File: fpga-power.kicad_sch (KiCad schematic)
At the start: 76 parts, among them U8 XC7K160T-FFG676

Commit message: [#65754] Rev 2.0.0 Initial commit - source design files from so-dimm-ddr5-tester e0a54f86
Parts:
- removed C100, C104, C114, C116, C118, C47, C51, C55, C57, C59, C61, C63, C65, C66, C67, C69, C70, C71, C73, C74, C75, C77, C78, C79, C81, C82, C83, C84, C85, C87, C88, C89, C91, C92, C93, C95, C96, C97, C98: C_100n_0201, data-center-rdimm-ddr5-tester-footprints:C_0201, symbol data-center-rdimm-ddr5-tester:C_100n_0201
- removed C101, C106, C107, C108, C109, C110, C111, C113, C115, C117, C48, C50, C52, C54, C56, C58, C62, C68, C72, C76, C80, C86, C90, C94, C99: C_4u7_0402, data-center-rdimm-ddr5-tester-footprints:C_0402_1005Metric, symbol data-center-rdimm-ddr5-tester:C_4u7_0402
- removed C102, C105: C_330u_KEMET_D, data-center-rdimm-ddr5-tester-footprints:KEMET_D, symbol data-center-rdimm-ddr5-tester:C_330u_KEMET_D
- removed C103, C119, C120, C121, C49, C53, C60, C64: C_47u_0603, data-center-rdimm-ddr5-tester-footprints:C_0603_1608Metric, symbol data-center-rdimm-ddr5-tester:C_47u_0603
- removed C112: C_100u_KEMET_A, data-center-rdimm-ddr5-tester-footprints:KEMET_A, symbol data-center-rdimm-ddr5-tester:C_100u_KEMET_A
- removed U8: XC7K160T-FFG676, data-center-rdimm-ddr5-tester-footprints:BGA-676_27x27mm_Layout26x26_P1X1mm, symbol data-center-rdimm-ddr5-tester:XC7K160T-FFG676
- added C100, C101, C104, C105, C106, C107, C108, C13, C19, C20, C21, C22, C23, C24, C26, C28, C29, C30, C31, C32, C33, C35, C36, C37, C39, C40, C41, C42, C44, C45, C46, C47, C48, C49, C51, C52, C53, C55, C56, C58, C59, C61, C63, C64, C65, C66, C68, C69, C70, C72, C74, C75, C76, C77, C78, C79, C80, C81, C82, C83, C84, C86, C87, C88, C89, C90, C91, C92, C93, C94, C95, C96, C98, C99: C_100n_0402, antmicro-footprints:C_0402_1005Metric, symbol antmicroCapacitors0402:C_100n_0402
- added C102, C103, C34, C43, C50, C57, C62, C67, C71, C97: C_4u7_0402, antmicro-footprints:C_0402_1005Metric, symbol antmicroCapacitors0402:C_4u7_0402
- added C11, C14, C15, C16, C17, C18, C27, C60, C73, C85: C_47u_0603, antmicro-footprints:C_0603_1608Metric, symbol antmicroCapacitors0603:C_47u_0603
- added C12: C_Pol_1m_2.5V_KEMET-T520-D, antmicro-footprints:C_Pol_EIA-D, symbol antmicroCapacitorspol:C_Pol_1m_2.5V_KEMET-T520-D
- added C25, C38: C_Pol_330u_6.3V_KEMET-T520-B, antmicro-footprints:C_Pol_EIA-B, symbol antmicroCapacitorspol:C_Pol_330u_6.3V_KEMET-T520-B
- added C54: C_100u_0805, antmicro-footprints:C_0805_2012Metric, symbol antmicroCapacitorsmisc:C_100u_0805
- added R39: R_100R_0402, antmicro-footprints:R_0402_1005Metric, symbol antmicroResistors0402:R_100R_0402
- added U4: XC7K160T-FFG676, antmicro-footprints:BGA-676_27x27mm_Layout26x26_P1x1mm_FFG676, symbol antmicroFPGAChips:XC7K160T-FFG676
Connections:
- net GND: now also C100.1, C101.1, C102.2, C103.2, C104.1, C105.1, C106.1, C107.1, C108.1, C11.2, C12.2, C13.1, C14.2, C15.2, C16.2, C17.2, C18.2, C19.1, C20.1, C21.1, C22.1, C23.1, C24.1, C25.2, C26.1, C27.2, C28.1, C29.1, C30.1, C31.1, C32.1, C33.1, C34.2, C35.1, C36.1, C37.1, C38.2, C39.1, C40.1, C41.1, C42.1, C43.2, C44.1, C45.1, C46.1, C47.1, C48.1, C49.1, C50.2, C51.1, C52.1, C53.1, C54.1, C55.1, C56.1, C57.2, C58.1, C59.1, C60.2, C61.1, C62.2, C63.1, C64.1, C65.1, C66.1, C67.2, C68.1, C69.1, C70.1, C71.2, C72.1, C73.2, C74.1, C75.1, C76.1, C77.1, C78.1, C79.1, C80.1, C81.1, C82.1, C83.1, C84.1, C85.2, C86.1, C87.1, C88.1, C89.1, C90.1, C91.1, C92.1, C93.1, C94.1, C95.1, C96.1, C97.2, C98.1, C99.1, U4.A1 (GND), U4.A16 (GND), U4.A2 (GND), U4.A26 (GND), U4.A5 (GND), U4.A6 (GND), U4.A7 (GND), U4.AA16 (GND), U4.AA26 (GND), U4.AA6 (GND), U4.AB13 (GND), U4.AB23 (GND), U4.AB3 (GND), U4.AC10 (GND), U4.AC20 (GND), U4.AD17 (GND), U4.AD7 (GND), U4.AE14 (GND), U4.AE24 (GND), U4.AE4 (GND), U4.AF1 (GND), U4.AF11 (GND), U4.AF21 (GND), U4.B13 (GND), U4.B23 (GND), U4.B4 (GND), U4.B7 (GND), U4.C1 (GND), U4.C10 (GND), U4.C20 (GND), U4.C5 (GND), U4.C7 (GND), U4.D17 (GND), U4.D4 (GND), U4.D7 (GND), U4.E1 (GND), U4.E14 (GND), U4.E2 (GND), U4.E24 (GND), U4.E5 (GND), U4.E7 (GND), U4.F11 (GND), U4.F21 (GND), U4.F3 (GND), U4.F4 (GND), U4.F7 (GND), U4.G1 (GND), U4.G18 (GND), U4.G5 (GND), U4.G8 (GND), U4.H15 (GND), U4.H25 (GND), U4.H4 (GND), U4.H7 (GND), U4.J1 (GND), U4.J12 (GND), U4.J2 (GND), U4.J22 (GND), U4.J5 (GND), U4.K11 (GND), U4.K13 (GND), U4.K19 (GND), U4.K3 (GND), U4.K4 (GND), U4.K7 (GND), U4.K9 (GND), U4.L1 (GND), U4.L10 (GND), U4.L12 (GND), U4.L14 (GND), U4.L16 (GND), U4.L26 (GND), U4.L5 (GND), U4.M11 (GNDADC_0), U4.M13 (GND), U4.M15 (GND), U4.M23 (GND), U4.M4 (GND), U4.M7 (GND), U4.M9 (GND), U4.N1 (GND), U4.N10 (GND), U4.N14 (GND), U4.N2 (GND), U4.N20 (GND), U4.N5 (GND), U4.N7 (GND), U4.P13 (GND), U4.P15 (GND), U4.P17 (GND), U4.P3 (GND), U4.P4 (GND), U4.P9 (GND), U4.R1 (GND), U4.R10 (GND), U4.R14 (GND), U4.R2 (GND), U4.R24 (GND), U4.R5 (GND), U4.R8 (GND), U4.T1 (GND), U4.T11 (GND), U4.T13 (GND), U4.T15 (GND), U4.T21 (GND), U4.T3 (GND), U4.T4 (GND), U4.T9 (GND), U4.U10 (GND), U4.U12 (GND), U4.U14 (GND), U4.U18 (GND), U4.U8 (GND), U4.V15 (GND), U4.V25 (GND), U4.V5 (GND), U4.W12 (GND), U4.W2 (GND), U4.W22 (GND), U4.Y19 (GND), U4.Y9 (GND)
- new net: R39.1, U4.M6 (MGTRREF_115)
- new net +1V0: C12.1, C13.2, C19.2, C25.1, C26.2, C33.2, C38.1, C42.2, C48.2, C54.2, C55.2, C61.2, C62.1, C65.2, C67.1, C70.2, C71.1, C75.2, C79.2, C83.2, C86.2, C88.2, C90.2, C92.2, U4.J9 (VCCINT), U4.K10 (VCCINT), U4.K12 (VCCINT), U4.K14 (VCCINT), U4.K8 (VCCINT), U4.L13 (VCCINT), U4.L15 (VCCINT), U4.L9 (VCCINT), U4.M14 (VCCINT), U4.M8 (VCCINT), U4.N13 (VCCBRAM), U4.N15 (VCCINT), U4.N9 (VCCINT), U4.P14 (VCCINT), U4.R13 (VCCBRAM), U4.R15 (VCCINT), U4.T12 (VCCBRAM), U4.T14 (VCCINT), U4.U13 (VCCBRAM), U4.U15 (VCCINT)
- new net +1V0_MGTAVCC: C100.2, C101.2, C102.1, C98.2, C99.2, U4.C6 (MGTAVCC), U4.E6 (MGTAVCC), U4.G6 (MGTAVCC), U4.J6 (MGTAVCC), U4.L6 (MGTAVCC)
- new net +1V1: C14.1, C20.2, C24.2, C31.2, C37.2, C44.2, C49.2, C60.1, C63.2, C66.2, C69.2, C74.2, C78.2, C82.2, C85.1, C87.2, C89.2, C91.2, C93.2, C94.2, C95.2
- new net +1V2_MGTAVTT: C103.1, C104.2, C105.2, C106.2, C107.2, C108.2, R39.2, U4.B3 (MGTAVTT), U4.C2 (MGTAVTT), U4.D3 (MGTAVTT), U4.G2 (MGTAVTT), U4.H3 (MGTAVTT), U4.L2 (MGTAVTT), U4.M3 (MGTAVTT), U4.M5 (MGTAVTTRCAL_115)
- new net +1V8: C11.1, C18.1, C27.1, C34.1, C43.1, C50.1, C57.1, C64.2, C68.2, C72.2, C77.2, C81.2, C84.2, C96.2, C97.1, U4.E8 (VCCBATT_0), U4.L11 (VCCAUX), U4.M10 (VCCAUX), U4.M12 (VCCADC_0), U4.N6 (MGTVCCAUX), U4.P10 (VCCAUX), U4.P8 (VCCAUX_IO_G0), U4.R9 (VCCAUX_IO_G0), U4.T10 (VCCAUX), U4.T8 (VCCAUX_IO_G0), U4.U11 (VCCAUX)
- new net +3V3: C15.1, C16.1, C17.1, C21.2, C22.2, C23.2, C28.2, C29.2, C30.2, C32.2, C35.2, C36.2, C39.2, C40.2, C41.2, C45.2, C46.2, C47.2, C51.2, C52.2, C53.2, C56.2, C58.2, C59.2, C73.1, C76.2, C80.2
- no-connect marks 45 -> 0
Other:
- note added: "BANK 0"
- note added: "BANK 12"
- note added: "BANK 14"
- note added: "BANK 16"
- note added: "BANK 32"
- note added: "BANK 33"
- note added: "BANK 34"
- note added: "Bank marked by dahed line referenced from 7 Series FPGAs PCB Design Guide UG483 (FFG+FBG Package worst case)"
- note added: "FPGA Power rails"
- note added: "MGT decoupling marked by dahed line referenced from 7 Series FPGAs PCB Design Guide UG482 (FFG+FBG Package worst case)"
- note added: "Trace length from the resistor pins to the FPGA pins MGTRREF and MGTAVTTRCAL must be equal in length."
- note added: "V_{CCAUX}"
- note added: "V_{CCBRAM}"
- note added: "V_{CCINT}"
- note removed: "Added capacitors coresponding to PCB Design Guide UG483"
- note removed: "Decoupling referenced from 7 Series FPGAs PCB Design Guide UG483 TODO: verify!"
- note removed: "POWER RAILS"
- note removed: "Place close to FPGA banks power supply"
- note removed: "UNUSED"
- title: Data Center RDIMM DDR5 Tester -> SO-DIMM DDR5 Tester

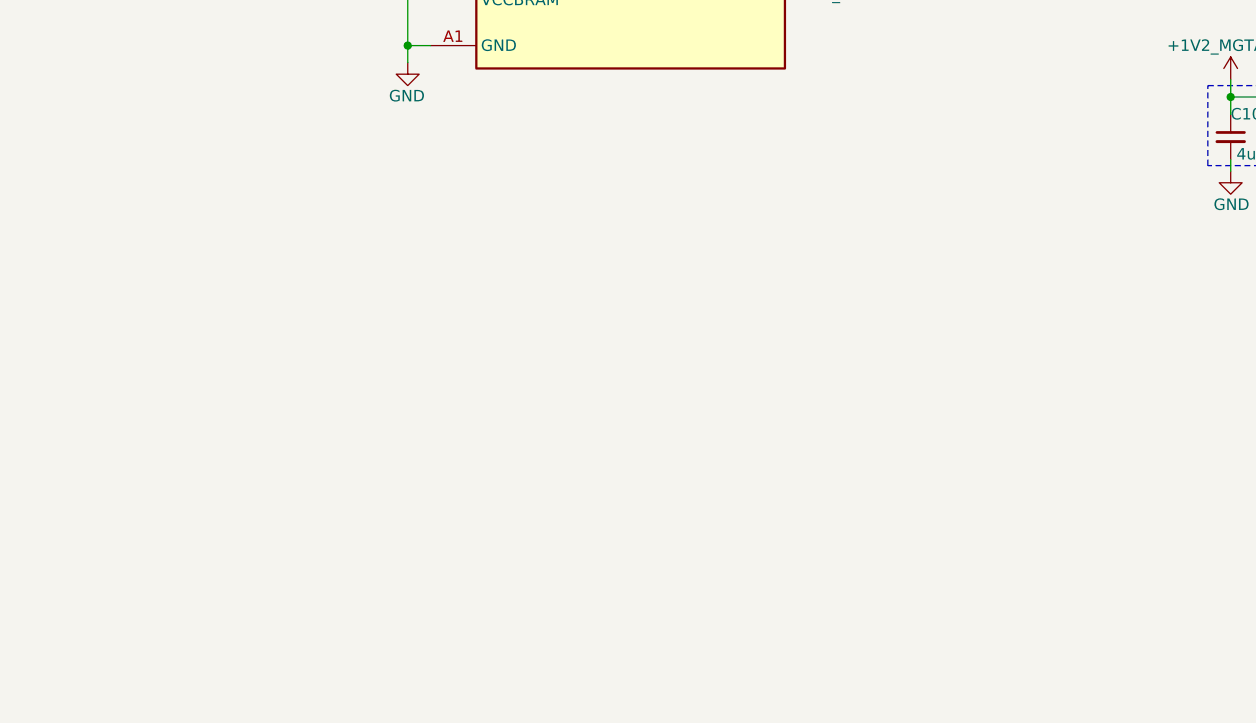
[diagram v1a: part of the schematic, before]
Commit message: [#66300] Add recommended FPGA supply voltages
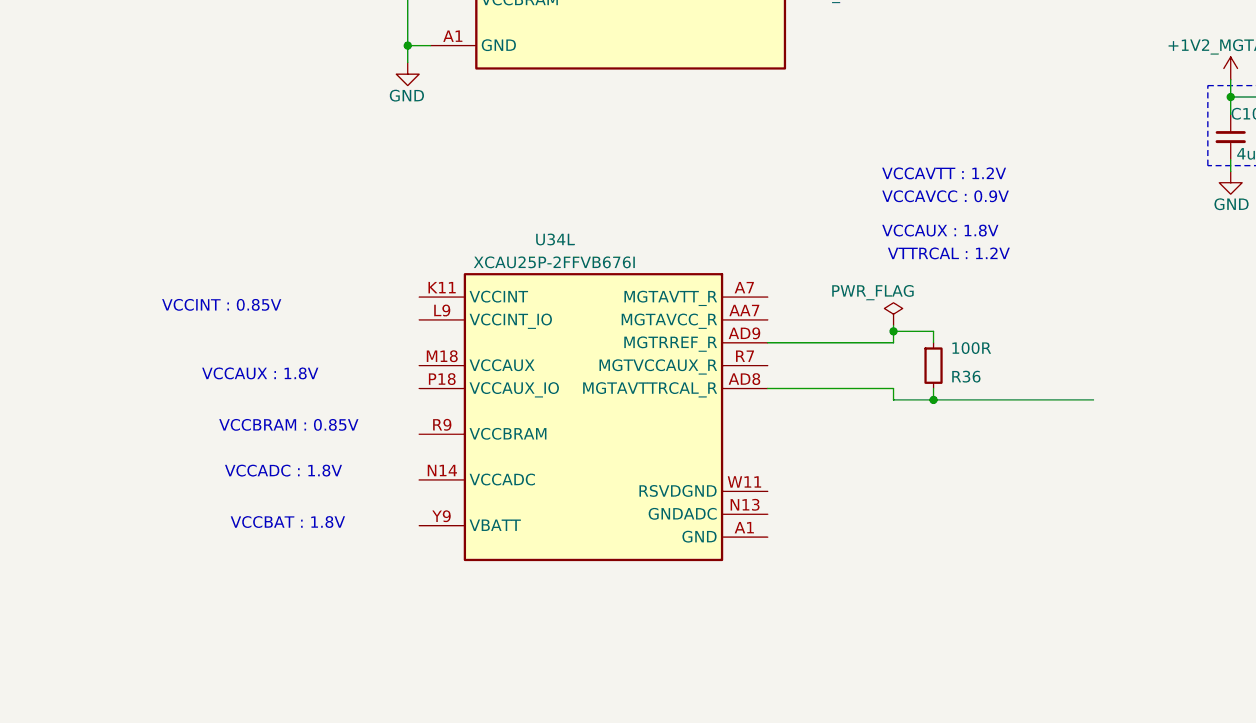
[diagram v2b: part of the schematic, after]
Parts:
- added R36: R_100R_0402, antmicro-footprints:R_0402_1005Metric, symbol antmicroResistors0402:R_100R_0402
- added U34: XCAU25P-2FFVB676I, antmicro-footprints:BGA-676_27x27mm_Layout26x26_P1x1mm_FFVB676, symbol antmicroFPGAChips:XCAU25P-2FFVB676I
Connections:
- new net: U34.A1 (GND), U34.A11 (GND), U34.A16 (GND), U34.A2 (GND), U34.A21 (GND), U34.A26 (GND), U34.A5 (GND), U34.A6 (GND), U34.A8 (GND), U34.AA1 (GND), U34.AA16 (GND), U34.AA2 (GND), U34.AA26 (GND), U34.AA3 (GND), U34.AA6 (GND), U34.AA8 (GND), U34.AB13 (GND), U34.AB23 (GND), U34.AB3 (GND), U34.AB4 (GND), U34.AB8 (GND), U34.AC1 (GND), U34.AC10 (GND), U34.AC2 (GND), U34.AC20 (GND), U34.AC25 (GND), U34.AC3 (GND), U34.AC6 (GND), U34.AC8 (GND), U34.AC9 (GND), U34.AD10 (GND), U34.AD17 (GND), U34.AD3 (GND), U34.AD4 (GND), U34.AD5 (GND), U34.AE1 (GND), U34.AE10 (GND), U34.AE14 (GND), U34.AE19 (GND), U34.AE2 (GND), U34.AE24 (GND), U34.AE5 (GND), U34.AE6 (GND), U34.AF10 (GND), U34.AF11 (GND), U34.AF16 (GND), U34.AF21 (GND), U34.AF26 (GND), U34.AF3 (GND), U34.AF4 (GND), U34.AF5 (GND), U34.AF8 (GND), U34.AF9 (GND), U34.B13 (GND), U34.B18 (GND), U34.B23 (GND), U34.B3 (GND), U34.B4 (GND), U34.B5 (GND), U34.B8 (GND), U34.C1 (GND), U34.C10 (GND), U34.C15 (GND), U34.C2 (GND), U34.C25 (GND), U34.C5 (GND), U34.C6 (GND), U34.C8 (GND), U34.D12 (GND), U34.D22 (GND), U34.D3 (GND), U34.D4 (GND), U34.D5 (GND), U34.D8 (GND), U34.E1 (GND), U34.E19 (GND), U34.E2 (GND), U34.E3 (GND), U34.E6 (GND), U34.E8 (GND), U34.F11 (GND), U34.F16 (GND), U34.F21 (GND), U34.F26 (GND), U34.F3 (GND), U34.F4 (GND), U34.F8 (GND), U34.G1 (GND), U34.G13 (GND), U34.G2 (GND), U34.G23 (GND), U34.G3 (GND), U34.G6 (GND), U34.G8 (GND), U34.H20 (GND), U34.H3 (GND), U34.H4 (GND), U34.H8 (GND), U34.J1 (GND), U34.J17 (GND), U34.J2 (GND), U34.J3 (GND), U34.J6 (GND), U34.J8 (GND), U34.K12 (GND), U34.K14 (GND), U34.K16 (GND), U34.K19 (GND), U34.K24 (GND), U34.K3 (GND), U34.K4 (GND), U34.K8 (GND), U34.L1 (GND), U34.L11 (GND), U34.L13 (GND), U34.L15 (GND), U34.L17 (GND), U34.L2 (GND), U34.L21 (GND), U34.L26 (GND), U34.L3 (GND), U34.L6 (GND), U34.L8 (GND), U34.M10 (GND), U34.M12 (GND), U34.M14 (GND), U34.M16 (GND), U34.M23 (GND), U34.M3 (GND), U34.M4 (GND), U34.M8 (GND), U34.N1 (GND), U34.N11 (GND), U34.N15 (GND), U34.N17 (GND), U34.N2 (GND), U34.N20 (GND), U34.N25 (GND), U34.N3 (GND), U34.N6 (GND), U34.N8 (GND), U34.P10 (GND), U34.P12 (GND), U34.P16 (GND), U34.P3 (GND), U34.P4 (GND), U34.P8 (GND), U34.R1 (GND), U34.R11 (GND), U34.R15 (GND), U34.R17 (GND), U34.R19 (GND), U34.R2 (GND), U34.R24 (GND), U34.R3 (GND), U34.R6 (GND), U34.R8 (GND), U34.T10 (GND), U34.T12 (GND), U34.T16 (GND), U34.T21 (GND), U34.T26 (GND), U34.T3 (GND), U34.T4 (GND), U34.T8 (GND), U34.U1 (GND), U34.U11 (GND), U34.U13 (GND), U34.U15 (GND), U34.U17 (GND), U34.U18 (GND), U34.U2 (GND), U34.U3 (GND), U34.U6 (GND), U34.U8 (GND), U34.V10 (GND), U34.V12 (GND), U34.V14 (GND), U34.V16 (GND), U34.V20 (GND), U34.V25 (GND), U34.V3 (GND), U34.V4 (GND), U34.V8 (GND), U34.W1 (GND), U34.W17 (GND), U34.W2 (GND), U34.W22 (GND), U34.W3 (GND), U34.W6 (GND), U34.W8 (GND), U34.Y19 (GND), U34.Y3 (GND), U34.Y4 (GND), U34.Y8 (GND)
- new net: U34.A7 (MGTAVTT_R), U34.AB5 (MGTAVTT_R), U34.AE7 (MGTAVTT_R), U34.C7 (MGTAVTT_R), U34.E7 (MGTAVTT_R), U34.F5 (MGTAVTT_R), U34.G7 (MGTAVTT_R), U34.H5 (MGTAVTT_R), U34.K5 (MGTAVTT_R), U34.M5 (MGTAVTT_R), U34.P5 (MGTAVTT_R), U34.T5 (MGTAVTT_R), U34.V5 (MGTAVTT_R), U34.Y5 (MGTAVTT_R)
- new net: U34.AA7 (MGTAVCC_R), U34.AC7 (MGTAVCC_R), U34.J7 (MGTAVCC_R), U34.L7 (MGTAVCC_R), U34.N7 (MGTAVCC_R), U34.W7 (MGTAVCC_R)
- new net: R36.2, U34.AD8 (MGTAVTTRCAL_R)
- new net: R36.1, U34.AD9 (MGTRREF_R)
- new net: U34.K11 (VCCINT), U34.K13 (VCCINT), U34.K15 (VCCINT), U34.K17 (VCCINT), U34.L10 (VCCINT), U34.L12 (VCCINT), U34.L14 (VCCINT), U34.L16 (VCCINT), U34.M11 (VCCINT), U34.M13 (VCCINT), U34.M15 (VCCINT), U34.M17 (VCCINT), U34.N10 (VCCINT), U34.N12 (VCCINT), U34.N16 (VCCINT), U34.P11 (VCCINT), U34.P15 (VCCINT), U34.P17 (VCCINT), U34.R10 (VCCINT), U34.R12 (VCCINT), U34.R16 (VCCINT), U34.T11 (VCCINT), U34.T15 (VCCINT), U34.T17 (VCCINT), U34.U10 (VCCINT), U34.U12 (VCCINT), U34.U14 (VCCINT), U34.U16 (VCCINT), U34.V11 (VCCINT), U34.V13 (VCCINT), U34.V15 (VCCINT), U34.V17 (VCCINT)
- new net: U34.L9 (VCCINT_IO), U34.M9 (VCCINT_IO), U34.N9 (VCCINT_IO), U34.P9 (VCCINT_IO)
- new net: U34.M18 (VCCAUX), U34.N18 (VCCAUX)
- new net: U34.P18 (VCCAUX_IO), U34.R18 (VCCAUX_IO), U34.T18 (VCCAUX_IO)
- new net: U34.R7 (MGTVCCAUX_R), U34.U7 (MGTVCCAUX_R)
- new net: U34.R9 (VCCBRAM), U34.T9 (VCCBRAM), U34.U9 (VCCBRAM), U34.V9 (VCCBRAM)
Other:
- note added: "VCCADC : 1.8V"
- note added: "VCCAUX : 1.8V"
- note added: "VCCAVCC : 0.9V"
- note added: "VCCAVTT : 1.2V"
- note added: "VCCBAT : 1.8V"
- note added: "VCCBRAM : 0.85V"
- note added: "VCCINT : 0.85V"
- note added: "VTTRCAL : 1.2V"

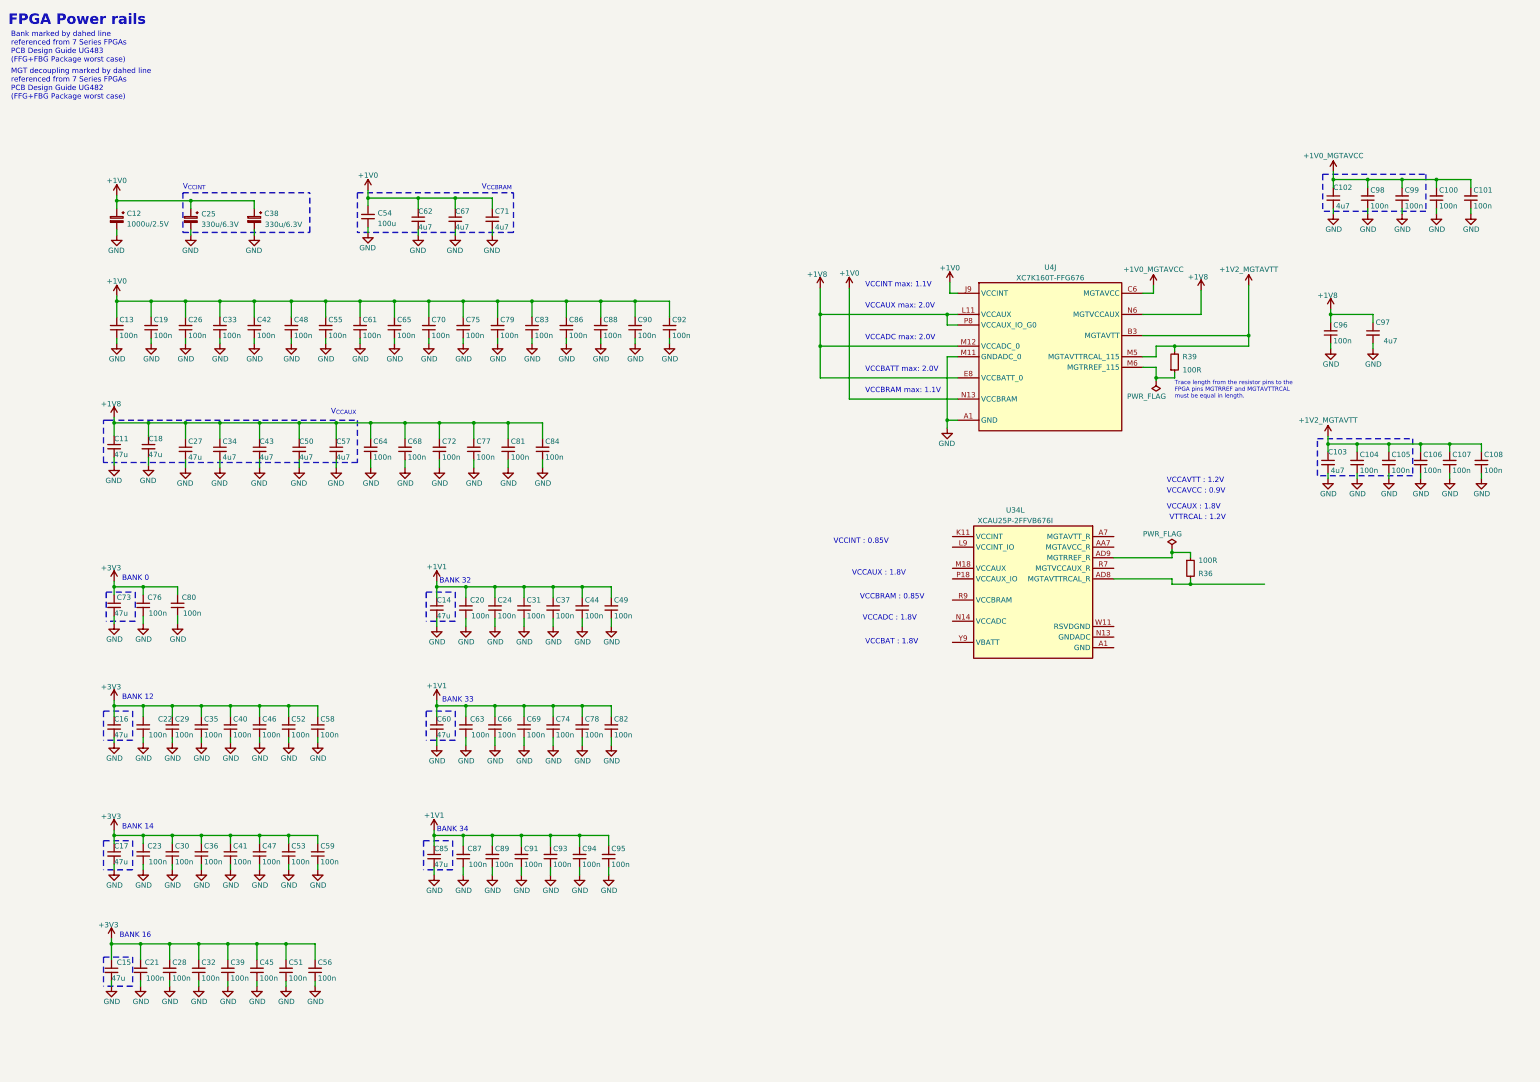
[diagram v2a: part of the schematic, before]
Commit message: [#66300] Connect supply domains to FPGA. Adjust decoupling
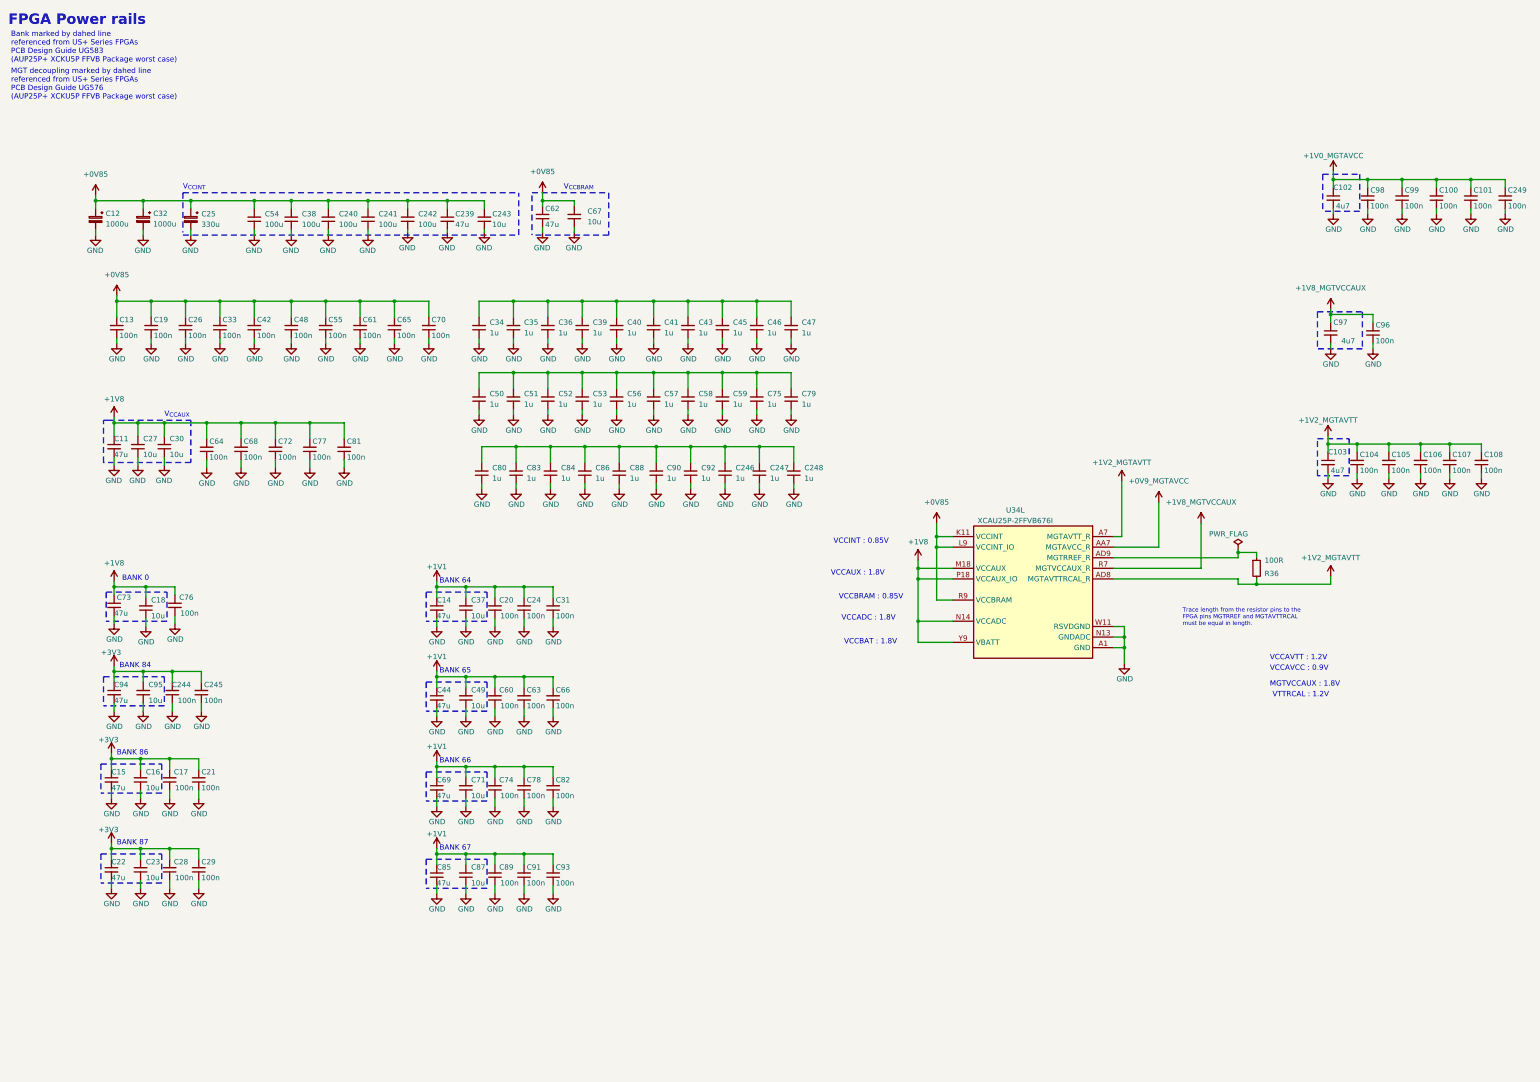
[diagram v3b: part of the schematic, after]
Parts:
- removed C16, C17, C18, C27, C60: C_47u_0603, antmicro-footprints:C_0603_1608Metric, symbol antmicroCapacitors0603:C_47u_0603
- removed C22, C23, C30, C32, C35, C36, C37, C39, C40, C41, C44, C45, C46, C47, C49, C51, C52, C53, C56, C58, C59, C69, C75, C79, C80, C83, C84, C86, C87, C88, C90, C92, C94, C95: C_100n_0402, antmicro-footprints:C_0402_1005Metric, symbol antmicroCapacitors0402:C_100n_0402
- removed C34, C43, C50, C57, C62, C67, C71: C_4u7_0402, antmicro-footprints:C_0402_1005Metric, symbol antmicroCapacitors0402:C_4u7_0402
- removed C38: C_Pol_330u_6.3V_KEMET-T520-B, antmicro-footprints:C_Pol_EIA-B, symbol antmicroCapacitorspol:C_Pol_330u_6.3V_KEMET-T520-B
- removed R39: R_100R_0402, antmicro-footprints:R_0402_1005Metric, symbol antmicroResistors0402:R_100R_0402
- removed U4: XC7K160T-FFG676, antmicro-footprints:BGA-676_27x27mm_Layout26x26_P1x1mm_FFG676, symbol antmicroFPGAChips:XC7K160T-FFG676
- added C16, C18, C23, C243, C27, C30, C37, C49, C67, C71, C87, C95: C_10u_10V_0402, antmicro-footprints:C_0402_1005Metric, symbol antmicroCapacitors0402:C_10u_10V_0402
- added C17, C244, C245, C249, C60: C_100n_0402, antmicro-footprints:C_0402_1005Metric, symbol antmicroCapacitors0402:C_100n_0402
- added C22, C239, C44, C62, C69, C94: C_47u_0603, antmicro-footprints:C_0603_1608Metric, symbol antmicroCapacitors0603:C_47u_0603
- added C240, C241, C242, C38: C_100u_0805, antmicro-footprints:C_0805_2012Metric, symbol antmicroCapacitorsmisc:C_100u_0805
- added C246, C247, C248, C34, C35, C36, C39, C40, C41, C43, C45, C46, C47, C50, C51, C52, C53, C56, C57, C58, C59, C75, C79, C80, C83, C84, C86, C88, C90, C92: C_1u_25V_0402, antmicro-footprints:C_0402_1005Metric, symbol antmicroCapacitors0402:C_1u_25V_0402
- added C32: C_Pol_1m_2.5V_KEMET-T520-D, antmicro-footprints:C_Pol_EIA-D, symbol antmicroCapacitorspol:C_Pol_1m_2.5V_KEMET-T520-D
- C12: Dielectric (none) -> template_dielectric; Val 1000u/2.5V -> 1000u
- C25: Dielectric (none) -> template_dielectric; Val 330u/6.3V -> 330u
- C54: Public (none) -> False
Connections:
- net +1V0 is gone; now on net +0V85: C12.1, C13.2, C19.2, C25.1, C26.2, C33.2, C42.2, C48.2, C54.2, C55.2, C61.2, C65.2, C70.2
- net +1V0_MGTAVCC: now also U34.AA7 (MGTAVCC_R), U34.AC7 (MGTAVCC_R), U34.J7 (MGTAVCC_R), U34.L7 (MGTAVCC_R), U34.N7 (MGTAVCC_R), U34.W7 (MGTAVCC_R), C249.2
- net +1V1: now also C37.2, C44.1, C49.2, C60.2, C69.1, C71.2, C87.2
- net +1V2_MGTAVTT: now also R36.2, U34.A7 (MGTAVTT_R), U34.AB5 (MGTAVTT_R), U34.AD8 (MGTAVTTRCAL_R), U34.AE7 (MGTAVTT_R), U34.C7 (MGTAVTT_R), U34.E7 (MGTAVTT_R), U34.F5 (MGTAVTT_R), U34.G7 (MGTAVTT_R), U34.H5 (MGTAVTT_R), U34.K5 (MGTAVTT_R), U34.M5 (MGTAVTT_R), U34.P5 (MGTAVTT_R), U34.T5 (MGTAVTT_R), U34.V5 (MGTAVTT_R), U34.Y5 (MGTAVTT_R)
- net +1V8: now also C73.1, C76.2, U34.M18 (VCCAUX), U34.N14 (VCCADC), U34.N18 (VCCAUX), U34.P18 (VCCAUX_IO), U34.R18 (VCCAUX_IO), U34.T18 (VCCAUX_IO), U34.Y9 (VBATT), C18.2, C27.2, C30.2; no longer C96.2, C97.1
- net +3V3: now also C16.2, C17.2, C22.1, C23.2, C244.2, C245.2, C94.1, C95.2; no longer C73.1, C76.2
- net GND: now also U34.A1 (GND), U34.A11 (GND), U34.A16 (GND), U34.A2 (GND), U34.A21 (GND), U34.A26 (GND), U34.A5 (GND), U34.A6 (GND), U34.A8 (GND), U34.AA1 (GND), U34.AA16 (GND), U34.AA2 (GND), U34.AA26 (GND), U34.AA3 (GND), U34.AA6 (GND), U34.AA8 (GND), U34.AB13 (GND), U34.AB23 (GND), U34.AB3 (GND), U34.AB4 (GND), U34.AB8 (GND), U34.AC1 (GND), U34.AC10 (GND), U34.AC2 (GND), U34.AC20 (GND), U34.AC25 (GND), U34.AC3 (GND), U34.AC6 (GND), U34.AC8 (GND), U34.AC9 (GND), U34.AD10 (GND), U34.AD17 (GND), U34.AD3 (GND), U34.AD4 (GND), U34.AD5 (GND), U34.AE1 (GND), U34.AE10 (GND), U34.AE14 (GND), U34.AE19 (GND), U34.AE2 (GND), U34.AE24 (GND), U34.AE5 (GND), U34.AE6 (GND), U34.AF10 (GND), U34.AF11 (GND), U34.AF16 (GND), U34.AF21 (GND), U34.AF26 (GND), U34.AF3 (GND), U34.AF4 (GND), U34.AF5 (GND), U34.AF8 (GND), U34.AF9 (GND), U34.B13 (GND), U34.B18 (GND), U34.B23 (GND), U34.B3 (GND), U34.B4 (GND), U34.B5 (GND), U34.B8 (GND), U34.C1 (GND), U34.C10 (GND), U34.C15 (GND), U34.C2 (GND), U34.C25 (GND), U34.C5 (GND), U34.C6 (GND), U34.C8 (GND), U34.D12 (GND), U34.D22 (GND), U34.D3 (GND), U34.D4 (GND), U34.D5 (GND), U34.D8 (GND), U34.E1 (GND), U34.E19 (GND), U34.E2 (GND), U34.E3 (GND), U34.E6 (GND), U34.E8 (GND), U34.F11 (GND), U34.F16 (GND), U34.F21 (GND), U34.F26 (GND), U34.F3 (GND), U34.F4 (GND), U34.F8 (GND), U34.G1 (GND), U34.G13 (GND), U34.G2 (GND), U34.G23 (GND), U34.G3 (GND), U34.G6 (GND), U34.G8 (GND), U34.H20 (GND), U34.H3 (GND), U34.H4 (GND), U34.H8 (GND), U34.J1 (GND), U34.J17 (GND), U34.J2 (GND), U34.J3 (GND), U34.J6 (GND), U34.J8 (GND), U34.K12 (GND), U34.K14 (GND), U34.K16 (GND), U34.K19 (GND), U34.K24 (GND), U34.K3 (GND), U34.K4 (GND), U34.K8 (GND), U34.L1 (GND), U34.L11 (GND), U34.L13 (GND), U34.L15 (GND), U34.L17 (GND), U34.L2 (GND), U34.L21 (GND), U34.L26 (GND), U34.L3 (GND), U34.L6 (GND), U34.L8 (GND), U34.M10 (GND), U34.M12 (GND), U34.M14 (GND), U34.M16 (GND), U34.M23 (GND), U34.M3 (GND), U34.M4 (GND), U34.M8 (GND), U34.N1 (GND), U34.N11 (GND), U34.N13 (GNDADC), U34.N15 (GND), U34.N17 (GND), U34.N2 (GND), U34.N20 (GND), U34.N25 (GND), U34.N3 (GND), U34.N6 (GND), U34.N8 (GND), U34.P10 (GND), U34.P12 (GND), U34.P16 (GND), U34.P3 (GND), U34.P4 (GND), U34.P8 (GND), U34.R1 (GND), U34.R11 (GND), U34.R15 (GND), U34.R17 (GND), U34.R19 (GND), U34.R2 (GND), U34.R24 (GND), U34.R3 (GND), U34.R6 (GND), U34.R8 (GND), U34.T10 (GND), U34.T12 (GND), U34.T16 (GND), U34.T21 (GND), U34.T26 (GND), U34.T3 (GND), U34.T4 (GND), U34.T8 (GND), U34.U1 (GND), U34.U11 (GND), U34.U13 (GND), U34.U15 (GND), U34.U17 (GND), U34.U18 (GND), U34.U2 (GND), U34.U3 (GND), U34.U6 (GND), U34.U8 (GND), U34.V10 (GND), U34.V12 (GND), U34.V14 (GND), U34.V16 (GND), U34.V20 (GND), U34.V25 (GND), U34.V3 (GND), U34.V4 (GND), U34.V8 (GND), U34.W1 (GND), U34.W11 (RSVDGND), U34.W17 (GND), U34.W2 (GND), U34.W22 (GND), U34.W3 (GND), U34.W6 (GND), U34.W8 (GND), U34.Y19 (GND), U34.Y3 (GND), U34.Y4 (GND), U34.Y8 (GND), C16.1, C17.1, C18.1, C22.2, C23.1, C239.2, C240.1, C241.1, C242.1, C243.1, C244.1, C245.1, C246.1, C247.1, C248.1, C249.1, C27.1, C30.1, C32.2, C34.1, C35.1, C36.1, C37.1, C38.1, C39.1, C40.1, C41.1, C43.1, C44.2, C45.1, C46.1, C47.1, C49.1, C50.1, C51.1, C52.1, C53.1, C56.1, C57.1, C58.1, C59.1, C60.1, C62.2, C67.1, C69.2, C71.1, C75.1, C79.1, C80.1, C83.1, C84.1, C86.1, C87.1, C88.1, C90.1, C92.1, C94.2, C95.1
- net +0V85: now reaches U34.K11 (VCCINT), U34.K13 (VCCINT), U34.K15 (VCCINT), U34.K17 (VCCINT), U34.L10 (VCCINT), U34.L12 (VCCINT), U34.L14 (VCCINT), U34.L16 (VCCINT), U34.M11 (VCCINT), U34.M13 (VCCINT), U34.M15 (VCCINT), U34.M17 (VCCINT), U34.N10 (VCCINT), U34.N12 (VCCINT), U34.N16 (VCCINT), U34.P11 (VCCINT), U34.P15 (VCCINT), U34.P17 (VCCINT), U34.R10 (VCCINT), U34.R12 (VCCINT), U34.R16 (VCCINT), U34.T11 (VCCINT), U34.T15 (VCCINT), U34.T17 (VCCINT), U34.U10 (VCCINT), U34.U12 (VCCINT), U34.U14 (VCCINT), U34.U16 (VCCINT), U34.V11 (VCCINT), U34.V13 (VCCINT), U34.V15 (VCCINT), U34.V17 (VCCINT)
- net +0V85: now also U34.L9 (VCCINT_IO), U34.M9 (VCCINT_IO), U34.N9 (VCCINT_IO), U34.P9 (VCCINT_IO), U34.R9 (VCCBRAM), U34.T9 (VCCBRAM), U34.U9 (VCCBRAM), U34.V9 (VCCBRAM), C239.1, C240.2, C241.2, C242.2, C243.2, C32.1, C38.2, C62.1, C67.2
- net +1V8_MGTVCCAUX: now reaches U34.R7 (MGTVCCAUX_R), U34.U7 (MGTVCCAUX_R)
- net +1V8_MGTVCCAUX: now also C96.2, C97.1
- new net: C50.2, C51.2, C52.2, C53.2, C56.2, C57.2, C58.2, C59.2, C75.2, C79.2
- new net: C34.2, C35.2, C36.2, C39.2, C40.2, C41.2, C43.2, C45.2, C46.2, C47.2
- new net: C246.2, C247.2, C248.2, C80.2, C83.2, C84.2, C86.2, C88.2, C90.2, C92.2
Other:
- note added: "BANK 64"
- note added: "BANK 65"
- note added: "BANK 66"
- note added: "BANK 67"
- note added: "BANK 84"
- note added: "BANK 86"
- note added: "BANK 87"
- note added: "Bank marked by dahed line referenced from US+ Series FPGAs PCB Design Guide UG583 (AUP25P+ XCKU5P FFVB Package worst case)"
- note added: "MGT decoupling marked by dahed line referenced from US+ Series FPGAs PCB Design Guide UG576 (AUP25P+ XCKU5P FFVB Package worst case)"
- note added: "MGTVCCAUX : 1.8V"
- note removed: "BANK 12"
- note removed: "BANK 14"
- note removed: "BANK 16"
- note removed: "BANK 32"
- note removed: "BANK 33"
- note removed: "BANK 34"
- note removed: "Bank marked by dahed line referenced from 7 Series FPGAs PCB Design Guide UG483 (FFG+FBG Package worst case)"
- note removed: "MGT decoupling marked by dahed line referenced from 7 Series FPGAs PCB Design Guide UG482 (FFG+FBG Package worst case)"
- note removed: "VCCADC max: 2.0V"
- note removed: "VCCAUX max: 2.0V"
- note removed: "VCCBATT max: 2.0V"
- note removed: "VCCBRAM max: 1.1V"
- note removed: "VCCINT max: 1.1V"
- title: SO-DIMM DDR5 Tester -> RDIMM DDR5 Tester
- moved on the sheet: C12, C20, C24, C31, C54, C64, C68, C72, C76, C77, C81, C96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
